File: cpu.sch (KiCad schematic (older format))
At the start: 15 parts, among them IC1 STM32L051K8T6, Q2 NMosfetGen, Q3 NMosfetGen, SW1 SW_PUSH

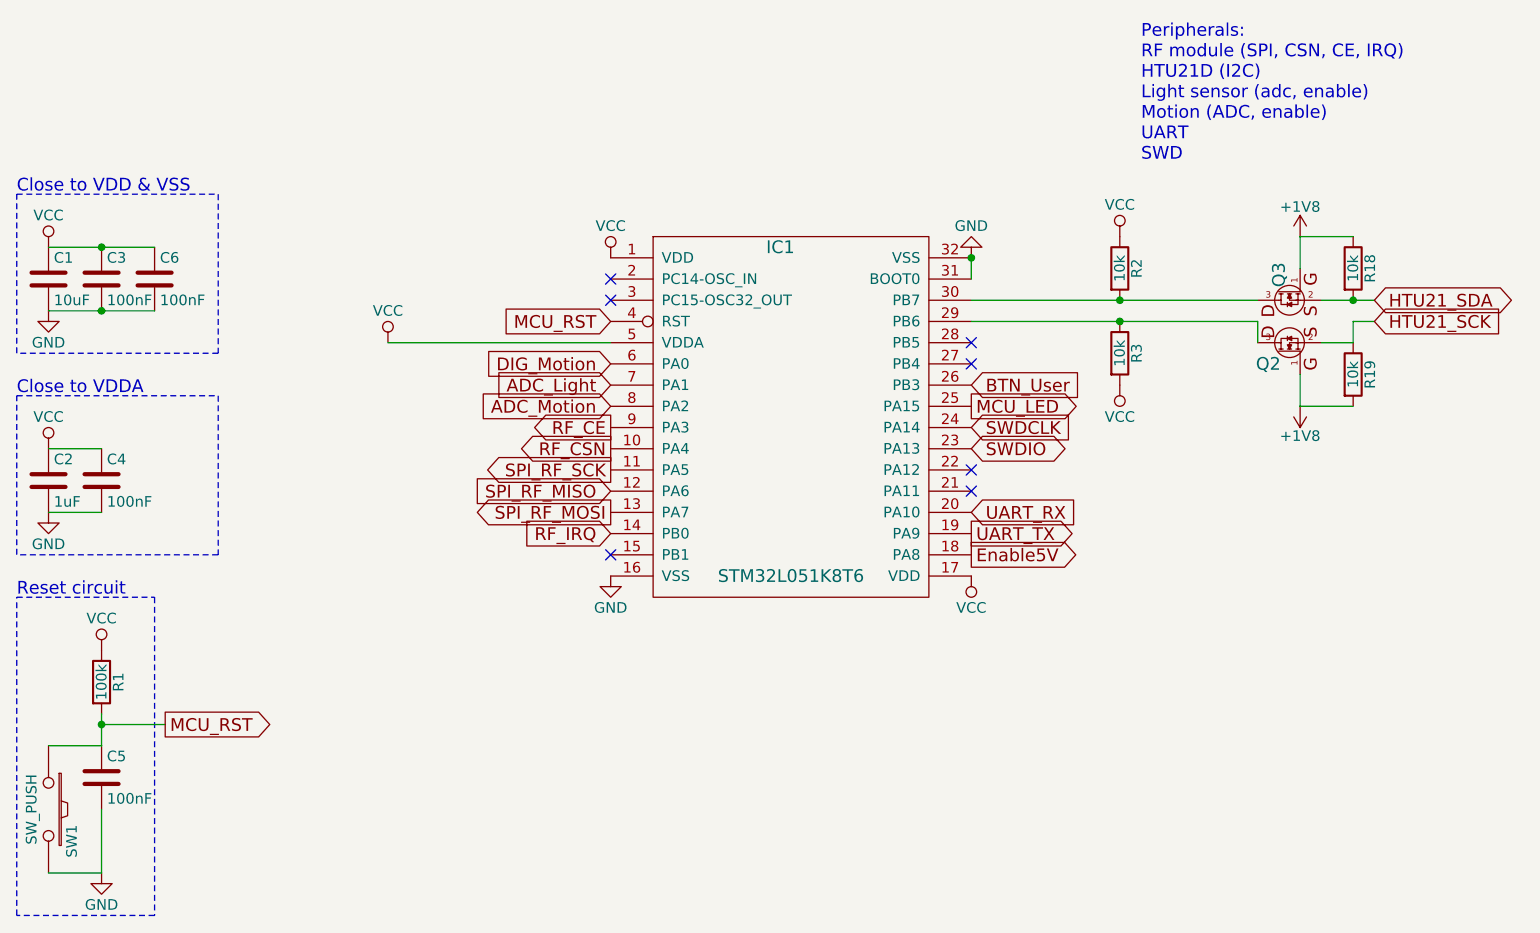
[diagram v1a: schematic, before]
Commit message: Add prices
Signed-off-by: Philip Luyckx <philip.luyckx@gmail.com>
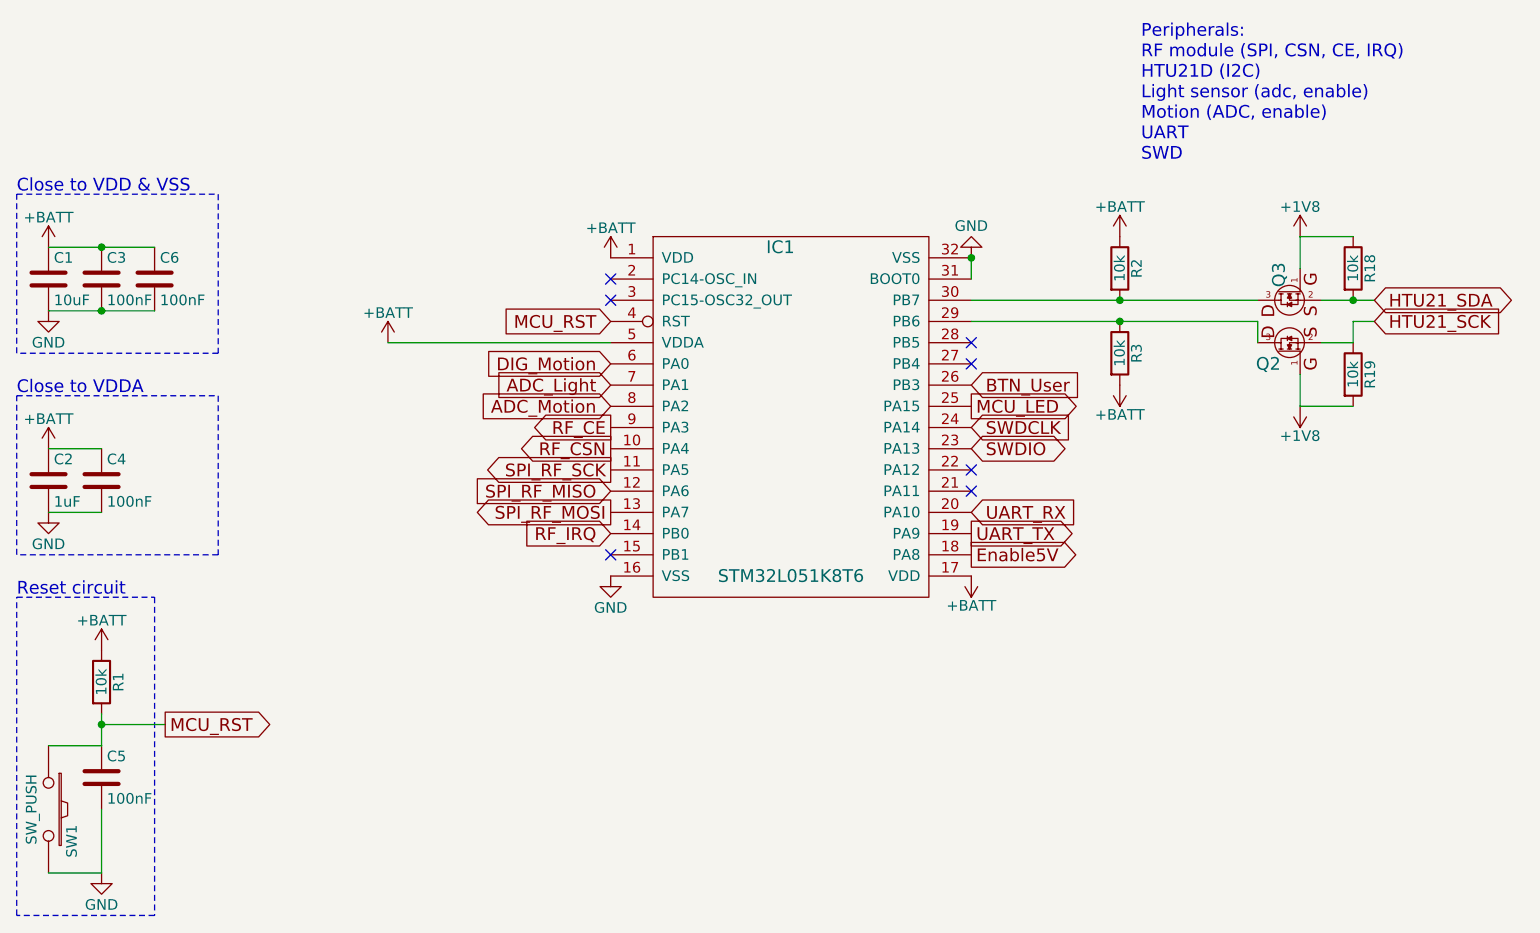
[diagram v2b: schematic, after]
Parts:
- Q2, Q3: Price (none) -> 0.02
- R1: value 100k -> 10k
- R18, R19, R2, R3: Price (none) -> 0.01
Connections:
- net VCC renamed +BATT
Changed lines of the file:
@@
 $EndDescr
 $Comp
-L VCC #PWR01
-U 1 1 565E0F45
-P 2700 3050
-F 0 "#PWR01" H 2700 2900 50  0001 C CNN
-F 1 "VCC" H 2700 3200 50  0000 C CNN
-F 2 "" H 2700 3050 60  0000 C CNN
-F 3 "" H 2700 3050 60  0000 C CNN
-	1    2700 3050
-	1    0    0    -1
-$EndComp
-$Comp
-L GND #PWR02
+L GND #PWR01
 U 1 1 565E0F59
 P 2700 3350
-F 0 "#PWR02" H 2700 3100 50  0001 C CNN
+F 0 "#PWR01" H 2700 3100 50  0001 C CNN
 F 1 "GND" H 2700 3200 50  0000 C CNN
 F 2 "" H 2700 3350 60  0000 C CNN
@@
 $EndComp
 $Comp
-L VCC #PWR03
-U 1 1 565E1082
-P 5350 3100
-F 0 "#PWR03" H 5350 2950 50  0001 C CNN
-F 1 "VCC" H 5350 3250 50  0000 C CNN
-F 2 "" H 5350 3100 60  0000 C CNN
-F 3 "" H 5350 3100 60  0000 C CNN
-	1    5350 3100
-	1    0    0    -1
-$EndComp
-$Comp
-L VCC #PWR04
-U 1 1 565E109E
-P 7050 4600
-F 0 "#PWR04" H 7050 4450 50  0001 C CNN
-F 1 "VCC" H 7050 4750 50  0000 C CNN
-F 2 "" H 7050 4600 60  0000 C CNN
-F 3 "" H 7050 4600 60  0000 C CNN
-	1    7050 4600
-	-1   0    0    1
-$EndComp
-$Comp
-L GND #PWR05
+L GND #PWR02
 U 1 1 565E10D6
 P 5350 4600
-F 0 "#PWR05" H 5350 4350 50  0001 C CNN
+F 0 "#PWR02" H 5350 4350 50  0001 C CNN
 F 1 "GND" H 5350 4450 50  0000 C CNN
 F 2 "" H 5350 4600 60  0000 C CNN
@@
 $EndComp
 $Comp
-L VCC #PWR06
-U 1 1 565E12D0
-P 2700 4000
-F 0 "#PWR06" H 2700 3850 50  0001 C CNN
-F 1 "VCC" H 2700 4150 50  0000 C CNN
-F 2 "" H 2700 4000 60  0000 C CNN
-F 3 "" H 2700 4000 60  0000 C CNN
-	1    2700 4000
-	1    0    0    -1
-$EndComp
-$Comp
-L GND #PWR07
+L GND #PWR03
 U 1 1 565E12F0
 P 2700 4300
-F 0 "#PWR07" H 2700 4050 50  0001 C CNN
+F 0 "#PWR03" H 2700 4050 50  0001 C CNN
 F 1 "GND" H 2700 4150 50  0000 C CNN
 F 2 "" H 2700 4300 60  0000 C CNN
@@
 P 2950 5100
 F 0 "R1" V 3030 5100 50  0000 C CNN
-F 1 "100k" V 2950 5100 50  0000 C CNN
+F 1 "10k" V 2950 5100 50  0000 C CNN
 F 2 "Resistors_SMD:R_0603" V 2880 5100 30  0001 C CNN
 F 3 "" H 2950 5100 30  0000 C CNN
@@
 $EndComp
 $Comp
-L VCC #PWR08
-U 1 1 565E15CE
-P 2950 4950
-F 0 "#PWR08" H 2950 4800 50  0001 C CNN
-F 1 "VCC" H 2950 5100 50  0000 C CNN
-F 2 "" H 2950 4950 60  0000 C CNN
-F 3 "" H 2950 4950 60  0000 C CNN
-	1    2950 4950
-	1    0    0    -1
-$EndComp
-$Comp
-L GND #PWR09
+L GND #PWR04
 U 1 1 565E15F4
 P 2950 6000
-F 0 "#PWR09" H 2950 5750 50  0001 C CNN
+F 0 "#PWR04" H 2950 5750 50  0001 C CNN
 F 1 "GND" H 2950 5850 50  0000 C CNN
 F 2 "" H 2950 6000 60  0000 C CNN
@@
 Text GLabel 5350 3400 0    60   Input ~ 0
 MCU_RST
-$Comp
-L VCC #PWR010
-U 1 1 565E178E
-P 4300 3500
-F 0 "#PWR010" H 4300 3350 50  0001 C CNN
-F 1 "VCC" H 4300 3650 50  0000 C CNN
-F 2 "" H 4300 3500 60  0000 C CNN
-F 3 "" H 4300 3500 60  0000 C CNN
-	1    4300 3500
-	1    0    0    -1
-$EndComp
 Text Notes 2550 4700 0    60   ~ 0
 Reset circuit
@@
 Enable5V
 $Comp
-L GND #PWR011
+L GND #PWR05
 U 1 1 565E10BA
 P 7050 3100
-F 0 "#PWR011" H 7050 2850 50  0001 C CNN
+F 0 "#PWR05" H 7050 2850 50  0001 C CNN
 F 1 "GND" H 7050 2950 50  0000 C CNN
 F 2 "" H 7050 3100 60  0000 C CNN
@@
 F 2 "Resistors_SMD:R_0603" V 7680 3150 50  0001 C CNN
 F 3 "" H 7750 3150 50  0000 C CNN
+F 4 "0.01" V 7750 3150 60  0001 C CNN "Price"
 	1    7750 3150
 	1    0    0    -1
 $EndComp
 Connection ~ 7750 3300
-$Comp
-L VCC #PWR012
-U 1 1 57536F05
-P 7750 3000
-F 0 "#PWR012" H 7750 2850 50  0001 C CNN
-F 1 "VCC" H 7750 3150 50  0000 C CNN
-F 2 "" H 7750 3000 50  0000 C CNN
-F 3 "" H 7750 3000 50  0000 C CNN
-	1    7750 3000
-	1    0    0    -1
-$EndComp
 $Comp
 L R R3
@@
 F 2 "Resistors_SMD:R_0603" V 7680 3550 50  0001 C CNN
 F 3 "" H 7750 3550 50  0000 C CNN
+F 4 "0.01" V 7750 3550 60  0001 C CNN "Price"
 	1    7750 3550
 	1    0    0    -1
-$EndComp
-$Comp
-L VCC #PWR013
-U 1 1 57536F6A
-P 7750 3700
-F 0 "#PWR013" H 7750 3550 50  0001 C CNN
-F 1 "VCC" H 7750 3850 50  0000 C CNN
-F 2 "" H 7750 3700 50  0000 C CNN
-F 3 "" H 7750 3700 50  0000 C CNN
-	1    7750 3700
-	-1   0    0    1
 $EndComp
 Connection ~ 7750 3400
@@
 F 2 "CustomSmd:SOT23" H 8500 3440 60  0001 C CNN
 F 3 "" H 8500 3440 60  0000 C CNN
+F 4 "0.02" V 8550 3300 60  0001 C CNN "Price"
 	1    8550 3300
 	0    -1   1    0
@@
 	8700 3300 8950 3300
 $Comp
-L +1V8 #PWR014
+L +1V8 #PWR06
 U 1 1 586E9891
 P 8600 3000
-F 0 "#PWR014" H 8600 2850 50  0001 C CNN
+F 0 "#PWR06" H 8600 2850 50  0001 C CNN
 F 1 "+1V8" H 8600 3140 50  0000 C CNN
 F 2 "" H 8600 3000 50  0000 C CNN
@@
 F 2 "Resistors_SMD:R_0603" V 8780 3150 50  0001 C CNN
 F 3 "" H 8850 3150 50  0000 C CNN
+F 4 "0.01" V 8850 3150 60  0001 C CNN "Price"
 	1    8850 3150
 	1    0    0    -1
@@
 F 2 "CustomSmd:SOT23" H 8500 3640 60  0001 C CNN
 F 3 "" H 8500 3640 60  0000 C CNN
+F 4 "0.02" H 8550 3500 60  0001 C CNN "Price"
 	1    8550 3500
 	0    -1   -1   0
@@
 F 2 "Resistors_SMD:R_0603" V 8780 3650 50  0001 C CNN
 F 3 "" H 8850 3650 50  0000 C CNN
+F 4 "0.01" V 8850 3650 60  0001 C CNN "Price"
 	1    8850 3650
 	1    0    0    -1
@@
 	8600 3800 8600 3650
 $Comp
-L +1V8 #PWR015
+L +1V8 #PWR07
 U 1 1 586E9BE5
 P 8600 3800
-F 0 "#PWR015" H 8600 3650 50  0001 C CNN
+F 0 "#PWR07" H 8600 3650 50  0001 C CNN
 F 1 "+1V8" H 8600 3940 50  0000 C CNN
 F 2 "" H 8600 3800 50  0000 C CNN
@@
 	-1   0    0    1
 $EndComp
+$Comp
+L +BATT #PWR08
+U 1 1 58A7875B
+P 5350 3100
+F 0 "#PWR08" H 5350 2950 50  0001 C CNN
+F 1 "+BATT" H 5350 3240 50  0000 C CNN
+F 2 "" H 5350 3100 50  0000 C CNN
+F 3 "" H 5350 3100 50  0000 C CNN
+	1    5350 3100
+	1    0    0    -1
+$EndComp
+$Comp
+L +BATT #PWR09
+U 1 1 58A78858
+P 7750 3000
+F 0 "#PWR09" H 7750 2850 50  0001 C CNN
+F 1 "+BATT" H 7750 3140 50  0000 C CNN
+F 2 "" H 7750 3000 50  0000 C CNN
+F 3 "" H 7750 3000 50  0000 C CNN
+	1    7750 3000
+	1    0    0    -1
+$EndComp
+$Comp
+L +BATT #PWR010
+U 1 1 58A788D3
+P 7050 4600
+F 0 "#PWR010" H 7050 4450 50  0001 C CNN
+F 1 "+BATT" H 7050 4740 50  0000 C CNN
+F 2 "" H 7050 4600 50  0000 C CNN
+F 3 "" H 7050 4600 50  0000 C CNN
+	1    7050 4600
+	-1   0    0    1
+$EndComp
+$Comp
+L +BATT #PWR011
+U 1 1 58A78AA5
+P 2700 3050
+F 0 "#PWR011" H 2700 2900 50  0001 C CNN
+F 1 "+BATT" H 2700 3190 50  0000 C CNN
+F 2 "" H 2700 3050 50  0000 C CNN
+F 3 "" H 2700 3050 50  0000 C CNN
+	1    2700 3050
+	1    0    0    -1
+$EndComp
+$Comp
+L +BATT #PWR012
+U 1 1 58A78AE7
+P 2700 4000
+F 0 "#PWR012" H 2700 3850 50  0001 C CNN
+F 1 "+BATT" H 2700 4140 50  0000 C CNN
+F 2 "" H 2700 4000 50  0000 C CNN
+F 3 "" H 2700 4000 50  0000 C CNN
+	1    2700 4000
+	1    0    0    -1
+$EndComp
+$Comp
+L +BATT #PWR013
+U 1 1 58A78B2B
+P 2950 4950
+F 0 "#PWR013" H 2950 4800 50  0001 C CNN
+F 1 "+BATT" H 2950 5090 50  0000 C CNN
+F 2 "" H 2950 4950 50  0000 C CNN
+F 3 "" H 2950 4950 50  0000 C CNN
+	1    2950 4950
+	1    0    0    -1
+$EndComp
+$Comp
+L +BATT #PWR014
+U 1 1 58A7944C
+P 4300 3500
+F 0 "#PWR014" H 4300 3350 50  0001 C CNN
+F 1 "+BATT" H 4300 3640 50  0000 C CNN
+F 2 "" H 4300 3500 50  0000 C CNN
+F 3 "" H 4300 3500 50  0000 C CNN
+	1    4300 3500
+	1    0    0    -1
+$EndComp
+$Comp
+L +BATT #PWR015
+U 1 1 58A7965D
+P 7750 3700
+F 0 "#PWR015" H 7750 3550 50  0001 C CNN
+F 1 "+BATT" H 7750 3840 50  0000 C CNN
+F 2 "" H 7750 3700 50  0000 C CNN
+F 3 "" H 7750 3700 50  0000 C CNN
+	1    7750 3700
+	-1   0    0    1
+$EndComp
